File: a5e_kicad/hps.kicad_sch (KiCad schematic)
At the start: 17 parts, among them J8 Micro_SD_Card, U11 NXS0506GUX, U40 TPS2116DRLR, U41 TPS22918DBVR, U7 A5EB013B-B23B

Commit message: Add LCSC part numbers and fix C102 footprint
Add a hidden LCSC field to 290 symbols from the JLCPCB parts match
(2026-10-23). Left without LCSC: U7, U15, L1 (not in the JLCPCB
library), C1/C2/C4 and L2-L5 (no value specified), J3 (no confident
match) and Y3 (the 12 pF Basic crystal does not suit the 27 pF load
caps). U2, U12, Y2 and J9 carry the exact-MPN LCSC numbers although
they currently show zero JLCPCB stock.

C102 (22U 6V3) had a 0201 footprint; no 22 uF 0201 part exists. Change
it to 0402 (C415703) like C5-C7.
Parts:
- C240, C241: LCSC (none) -> C52923
- C242, C244: LCSC (none) -> C19666
- C243, C245, C248: LCSC (none) -> C1525
- C246, C247: LCSC (none) -> C19702
- J8: LCSC (none) -> C5912397
- R241, R242, R243: LCSC (none) -> C25741
- U11: LCSC (none) -> C27795240
- U40: LCSC (none) -> C3235557
- U41: LCSC (none) -> C131941
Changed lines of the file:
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@@
 			)
 		)
+		(property "LCSC" "C19666"
+			(at 40.64 185.42 0)
+			(hide yes)
+			(show_name no)
+			(do_not_autoplace no)
+			(effects
+				(font
+					(size 1.27 1.27)
+				)
+			)
+		)
 		(property "Datasheet" "~"
 			(at 40.64 185.42 0)
@@
 			)
 		)
+		(property "LCSC" "C131941"
+			(at 137.16 165.1 0)
+			(hide yes)
+			(show_name no)
+			(do_not_autoplace no)
+			(effects
+				(font
+					(size 1.27 1.27)
+				)
+			)
+		)
 		(property "Datasheet" "https://www.ti.com/lit/ds/symlink/tps22918.pdf"
 			(at 137.16 165.1 0)
@@
 			)
 		)
+		(property "LCSC" "C25741"
+			(at 107.95 161.29 0)
+			(hide yes)
+			(show_name no)
+			(do_not_autoplace no)
+			(effects
+				(font
+					(size 1.27 1.27)
+				)
+			)
+		)
 		(property "Datasheet" "~"
 			(at 107.95 161.29 0)
@@
 			)
 		)
+		(property "LCSC" "C25741"
+			(at 24.13 148.59 0)
+			(hide yes)
+			(show_name no)
+			(do_not_autoplace no)
+			(effects
+				(font
+					(size 1.27 1.27)
+				)
+			)
+		)
 		(property "Datasheet" "~"
 			(at 24.13 148.59 0)
@@
 			)
 		)
+		(property "LCSC" "C1525"
+			(at 100.33 185.42 0)
+			(hide yes)
+			(show_name no)
+			(do_not_autoplace no)
+			(effects
+				(font
+					(size 1.27 1.27)
+				)
+			)
+		)
 		(property "Datasheet" "~"
 			(at 100.33 185.42 0)
@@
 			)
 		)
+		(property "LCSC" "C52923"
+			(at 27.94 185.42 0)
+			(hide yes)
+			(show_name no)
+			(do_not_autoplace no)
+			(effects
+				(font
+					(size 1.27 1.27)
+				)
+			)
+		)
 		(property "Datasheet" "~"
 			(at 27.94 185.42 0)
@@
 			)
 		)
+		(property "LCSC" "C19702"
+			(at 81.28 185.42 0)
+			(hide yes)
+			(show_name no)
+			(do_not_autoplace no)
+			(effects
+				(font
+					(size 1.27 1.27)
+				)
+			)
+		)
 		(property "Datasheet" "~"
 			(at 81.28 185.42 0)
@@
 			)
 		)
+		(property "LCSC" "C3235557"
+			(at 54.61 149.86 0)
+			(hide yes)
+			(show_name no)
+			(do_not_autoplace no)
+			(effects
+				(font
+					(size 1.27 1.27)
+				)
+			)
+		)
 		(property "Datasheet" "https://www.ti.com/lit/ds/symlink/tps2116.pdf"
 			(at 54.61 149.86 0)
@@
 			)
 		)
+		(property "LCSC" "C19702"
+			(at 92.71 185.42 0)
+			(hide yes)
+			(show_name no)
+			(do_not_autoplace no)
+			(effects
+				(font
+					(size 1.27 1.27)
+				)
+			)
+		)
 		(property "Datasheet" "~"
 			(at 92.71 185.42 0)
@@
 			)
 		)
+		(property "LCSC" "C19666"
+			(at 66.04 185.42 0)
+			(hide yes)
+			(show_name no)
+			(do_not_autoplace no)
+			(effects
+				(font
+					(size 1.27 1.27)
+				)
+			)
+		)
 		(property "Datasheet" "~"
 			(at 66.04 185.42 0)
@@
 			)
 		)
+		(property "LCSC" "C1525"
+			(at 48.26 185.42 0)
+			(hide yes)
+			(show_name no)
+			(do_not_autoplace no)
+			(effects
+				(font
+					(size 1.27 1.27)
+				)
+			)
+		)
 		(property "Datasheet" "~"
 			(at 48.26 185.42 0)
@@
 			)
 		)
+		(property "LCSC" "C25741"
+			(at 16.51 151.13 0)
+			(hide yes)
+			(show_name no)
+			(do_not_autoplace no)
+			(effects
+				(font
+					(size 1.27 1.27)
+				)
+			)
+		)
 		(property "Datasheet" "~"
 			(at 16.51 151.13 0)
@@
 			)
 		)
+		(property "LCSC" "C52923"
+			(at 20.32 185.42 0)
+			(hide yes)
+			(show_name no)
+			(do_not_autoplace no)
+			(effects
+				(font
+					(size 1.27 1.27)
+				)
+			)
+		)
 		(property "Datasheet" "~"
 			(at 20.32 185.42 0)
@@
 			)
 		)
+		(property "LCSC" "C1525"
+			(at 73.66 185.42 0)
+			(hide yes)
+			(show_name no)
+			(do_not_autoplace no)
+			(effects
+				(font
+					(size 1.27 1.27)
+				)
+			)
+		)
 		(property "Datasheet" "~"
 			(at 73.66 185.42 0)
@@
 			)
 		)
+		(property "LCSC" "C27795240"
+			(at 55.88 100.33 0)
+			(hide yes)
+			(show_name no)
+			(do_not_autoplace no)
+			(effects
+				(font
+					(size 1.27 1.27)
+				)
+			)
+		)
 		(property "Datasheet" "https://assets.nexperia.com/documents/data-sheet/NXS0506.pdf"
 			(at 55.88 100.33 0)
@@
 			(at 140.97 55.88 0)
 			(hide yes)
+			(show_name no)
+			(do_not_autoplace no)
+			(effects
+				(font
+					(size 1.27 1.27)
+				)
+			)
+		)
+		(property "LCSC" "C5912397"
+			(at 140.97 55.88 0)
+			(hide yes)

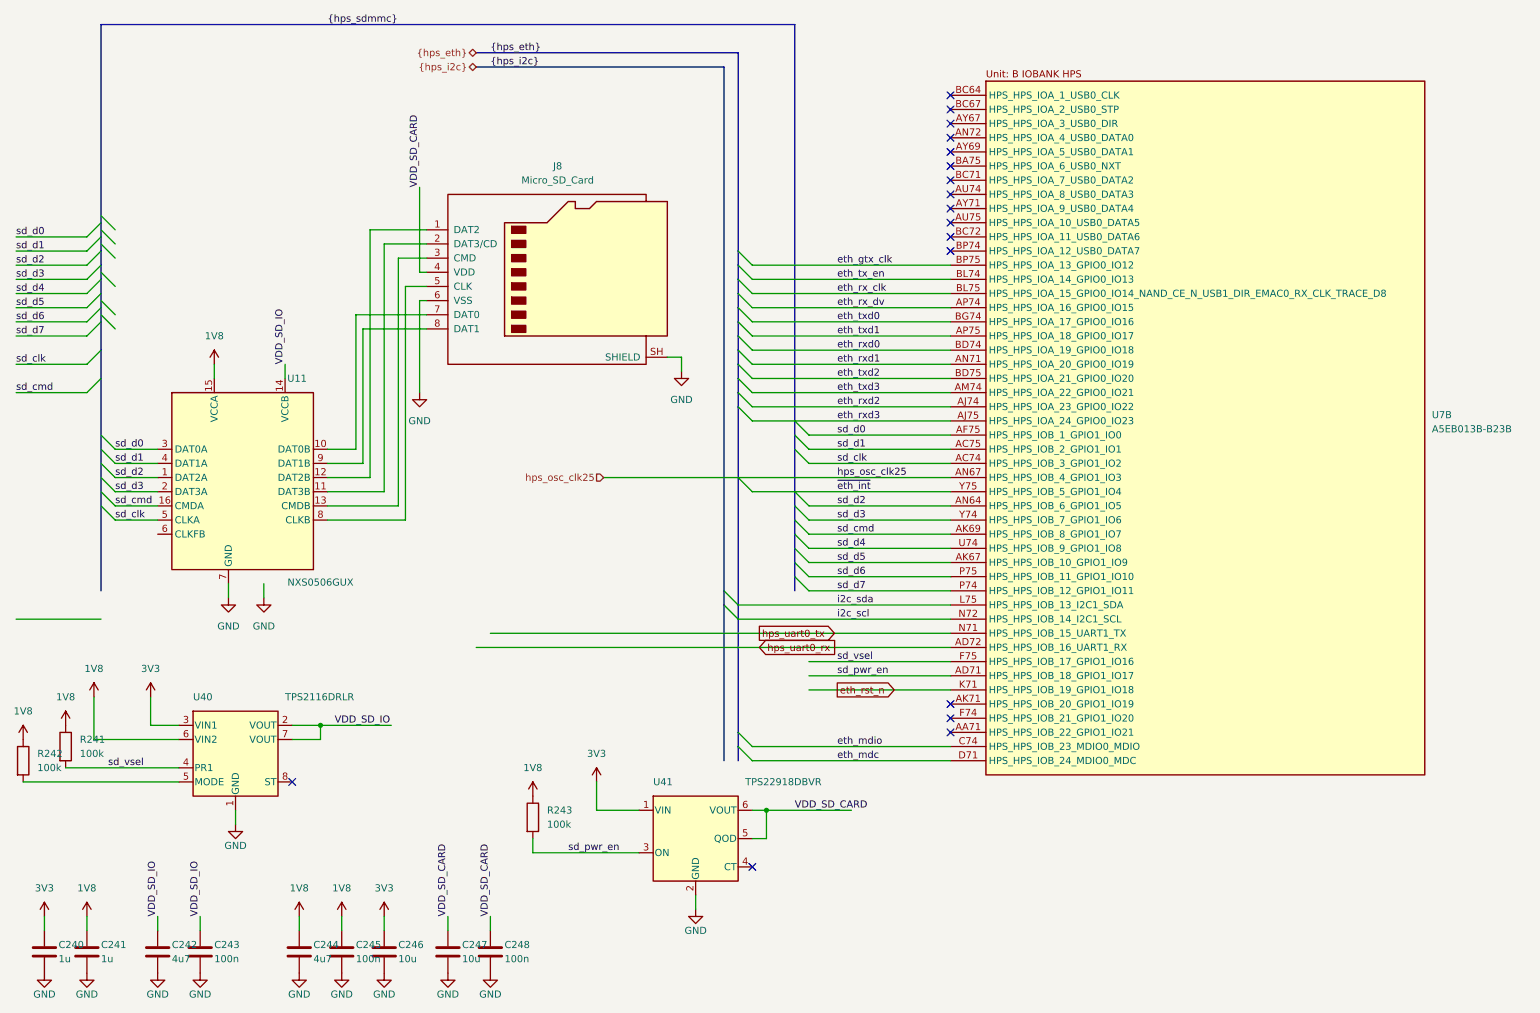
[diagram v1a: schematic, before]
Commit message: Replace microSD with KIOXIA THGAMVG7T13BAIL eMMC (1.8 V, no level translator)
U11 is now the eMMC (LFBGA-153), 8-bit bus direct to the HPS SD/MMC pins.
Removed J8, U40, U41, C240, C241, C247, C248 and the VDD_SD_IO/VDD_SD_CARD rails.
10k pull-ups on CMD/DAT0-7, RST_n on GPIO1_IO17 (emmc_rst_n), DS pulled down.
PCB not synced yet.
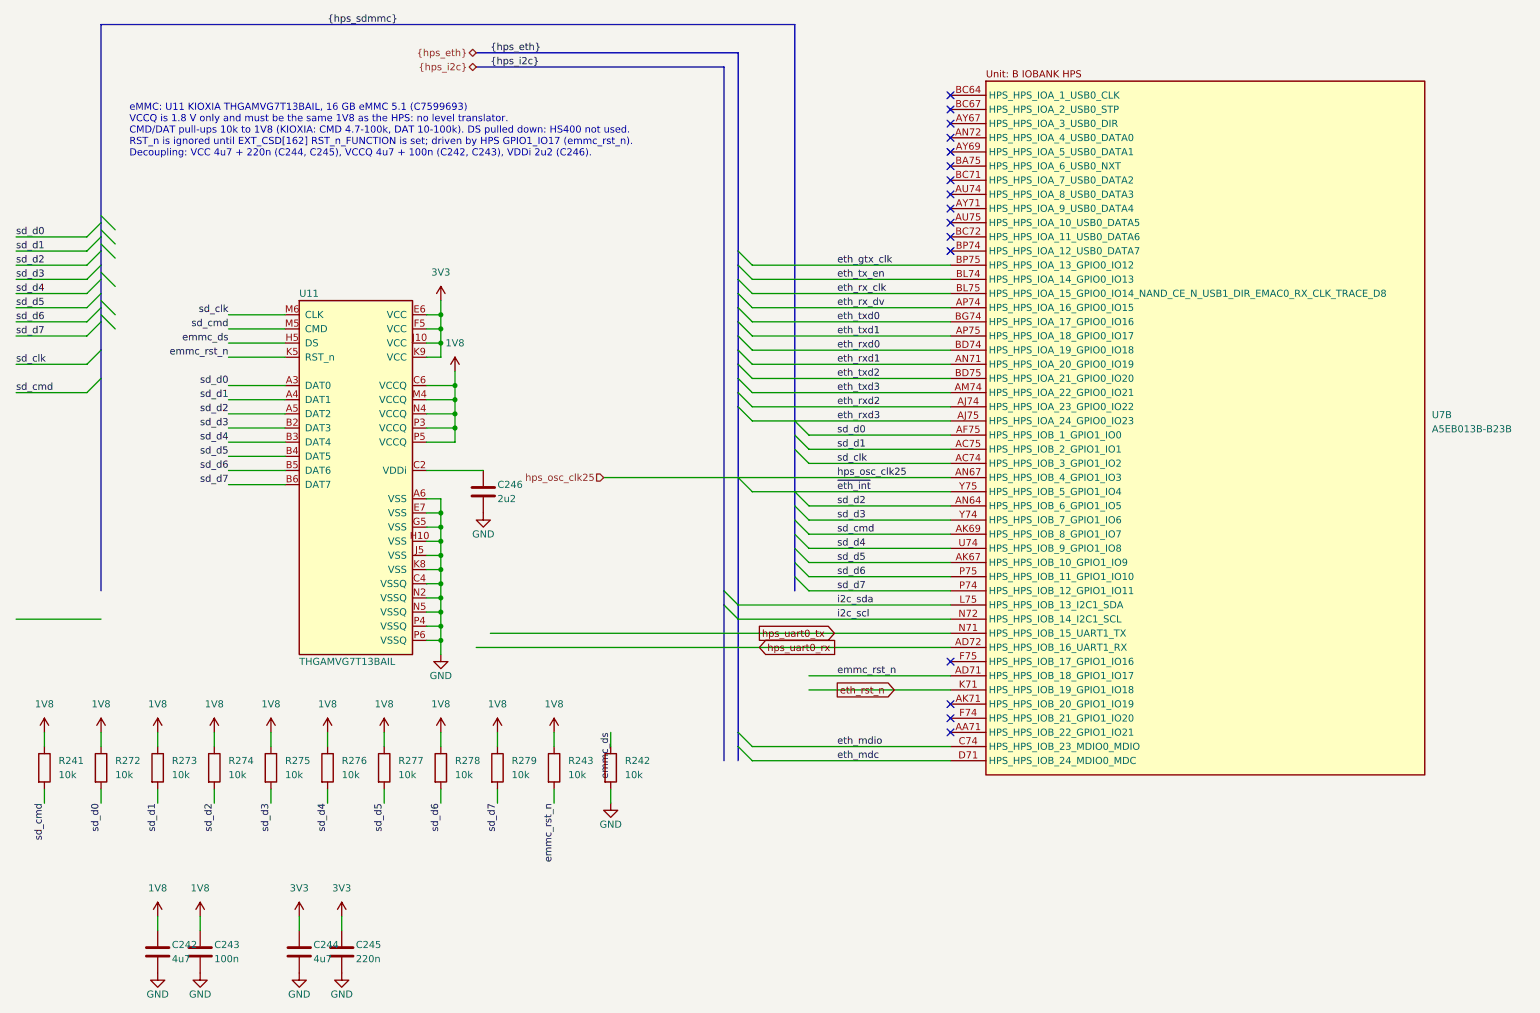
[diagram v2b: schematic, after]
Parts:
- removed C240, C241: 1u, Capacitor_SMD:C_0402_1005Metric, symbol Device:C
- removed C247: 10u, Capacitor_SMD:C_0603_1608Metric, symbol Device:C
- removed C248: 100n, Capacitor_SMD:C_0402_1005Metric, symbol Device:C
- removed J8: Micro_SD_Card, Connector_Card:microSD_HC_Wuerth_693072010801, symbol Connector:Micro_SD_Card
- removed U11: NXS0506GUX, agilex_lib:NXS0506GU_XQFN16_1.8x2.6mm_P0.4mm, symbol agilex_5_lib:NXS0506GU
- removed U40: TPS2116DRLR, Package_TO_SOT_SMD:SOT-583-8, symbol agilex_5_lib:TPS2116DRL
- removed U41: TPS22918DBVR, Package_TO_SOT_SMD:SOT-23-6, symbol agilex_5_lib:TPS22918DBV
- added R272, R273, R274, R275, R276, R277, R278, R279: 10k, Resistor_SMD:R_0402_1005Metric, symbol Device:R
- added U11: THGAMVG7T13BAIL, Package_BGA:LFBGA-153_11.5x13mm_Layout14x14_P0.5mm, symbol agilex_5_lib:THGAMVG7T13BAIL
- C245: value 100n -> 220n; LCSC C1525 -> C16772
- C246: value 10u -> 2u2; footprint Capacitor_SMD:C_0603_1608Metric -> Capacitor_SMD:C_0402_1005Metric; LCSC C19702 -> C12530
- R241, R242, R243: value 100k -> 10k; LCSC C25741 -> C25744
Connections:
- net VDD_SD_IO is gone; now on net 1V8: C242.1, C243.1
- net 1V8: now also R272.1, R273.1, R274.1, R275.1, R276.1, R277.1, R278.1, R279.1, U11.C6 (VCCQ), U11.M4 (VCCQ), U11.N4 (VCCQ), U11.P3 (VCCQ), U11.P5 (VCCQ); no longer C244.1, C245.1, R242.1
- net 3V3: now also C244.1, C245.1, U11.E6 (VCC), U11.F5 (VCC), U11.J10 (VCC), U11.K9 (VCC); no longer C246.1
- net GND: now also R242.2, U11.A6 (VSS), U11.C4 (VSSQ), U11.E7 (VSS), U11.G5 (VSS), U11.H10 (VSS), U11.J5 (VSS), U11.K8 (VSS), U11.N2 (VSSQ), U11.N5 (VSSQ), U11.P4 (VSSQ), U11.P6 (VSSQ)
- net sd_clk: now also U11.M6 (CLK)
- net sd_cmd: now also R241.2, U11.M5 (CMD)
- net sd_d0: now also R272.2, U11.A3 (DAT0)
- net sd_d1: now also R273.2, U11.A4 (DAT1)
- net sd_d2: now also R274.2, U11.A5 (DAT2)
- net sd_d3: now also R275.2, U11.B2 (DAT3)
- net sd_d4: now also R276.2, U11.B3 (DAT4)
- net sd_d5: now also R277.2, U11.B4 (DAT5)
- net sd_d6: now also R278.2, U11.B5 (DAT6)
- net sd_d7: now also R279.2, U11.B6 (DAT7)
- net sd_pwr_en renamed emmc_rst_n
- net emmc_rst_n: now also U11.K5 (RST_n)
- net sd_vsel: no longer names the net of U7.F75 (HPS_HPS_IOB_17_GPIO1_IO16)
- net sd_vsel: no longer R241.2
- new net: C246.1, U11.C2 (VDDi)
- new net emmc_ds: R242.1, U11.H5 (DS)
- no-connect marks 17 -> 16
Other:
- note added: "eMMC: U11 KIOXIA THGAMVG7T13BAIL, 16 GB eMMC 5.1 (C7599693) VCCQ is 1.8 V only and must be the same 1V8 as the HPS: no level translator. CMD/DAT pull-ups 10k to 1V8 (KIOXIA: CMD 4.7-100k, DAT 10-100k). DS pulled down: HS400 not used. RST_n is ignored until EXT_CSD[162] RST_n_FUNCTION is set; driven by HPS GPIO1_IO17 (emmc_rst_n). Decoupling: VCC 4u7 + 220n (C244, C245), VCCQ 4u7 + 100n (C242, C24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"
